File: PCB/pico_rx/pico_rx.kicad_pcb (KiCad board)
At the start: 2 copper layers, 54.6 x 89.5 mm, 77 parts, among them J1 Speaker, J2 Headphone, J4 I2C Display, J5 Antenna, J6 Battery, SW1 RotaryEncoder_Switch, SW2 SW_Push, SW3 SW_Push, SW4 SW_SPDT, U1 74CBT3251, U2 74CBT3251, U3 LTC6227, U4 FST3253, U5 Pico, U6 LTC6226xS8

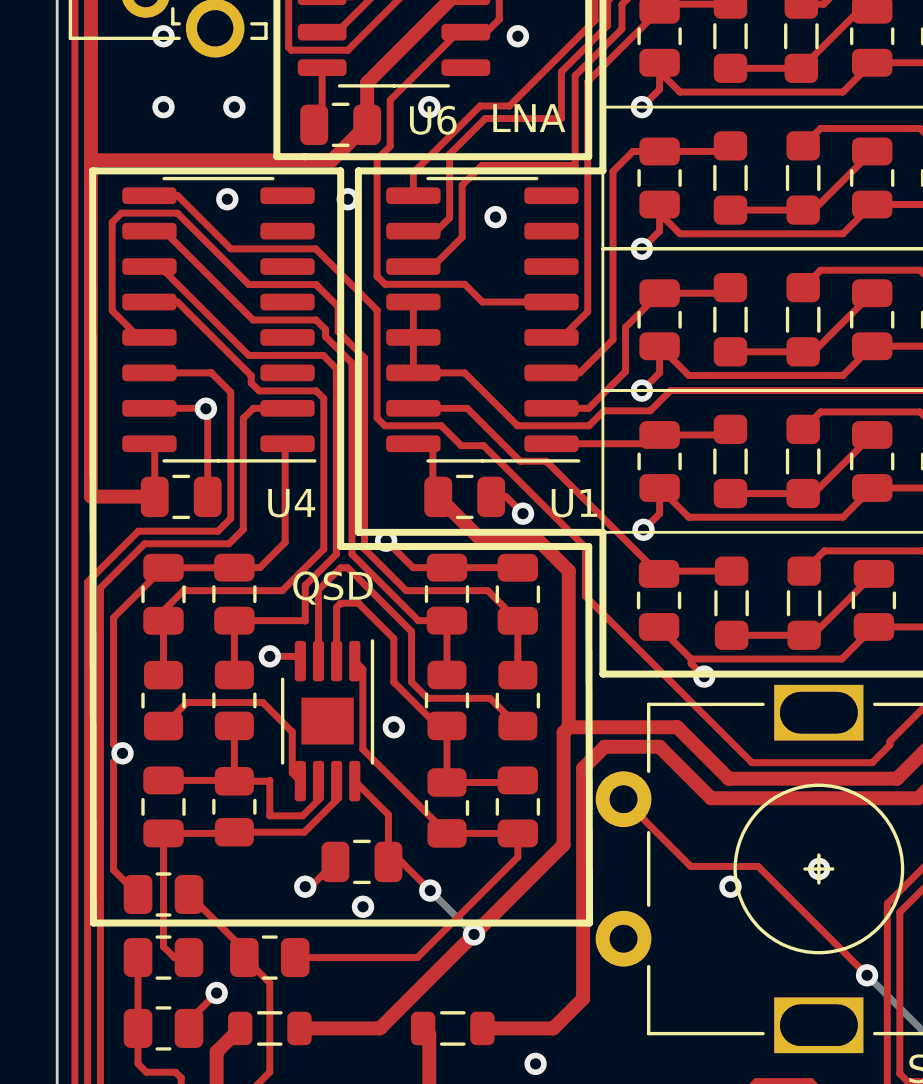
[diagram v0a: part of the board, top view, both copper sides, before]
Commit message: Correct error in schematic
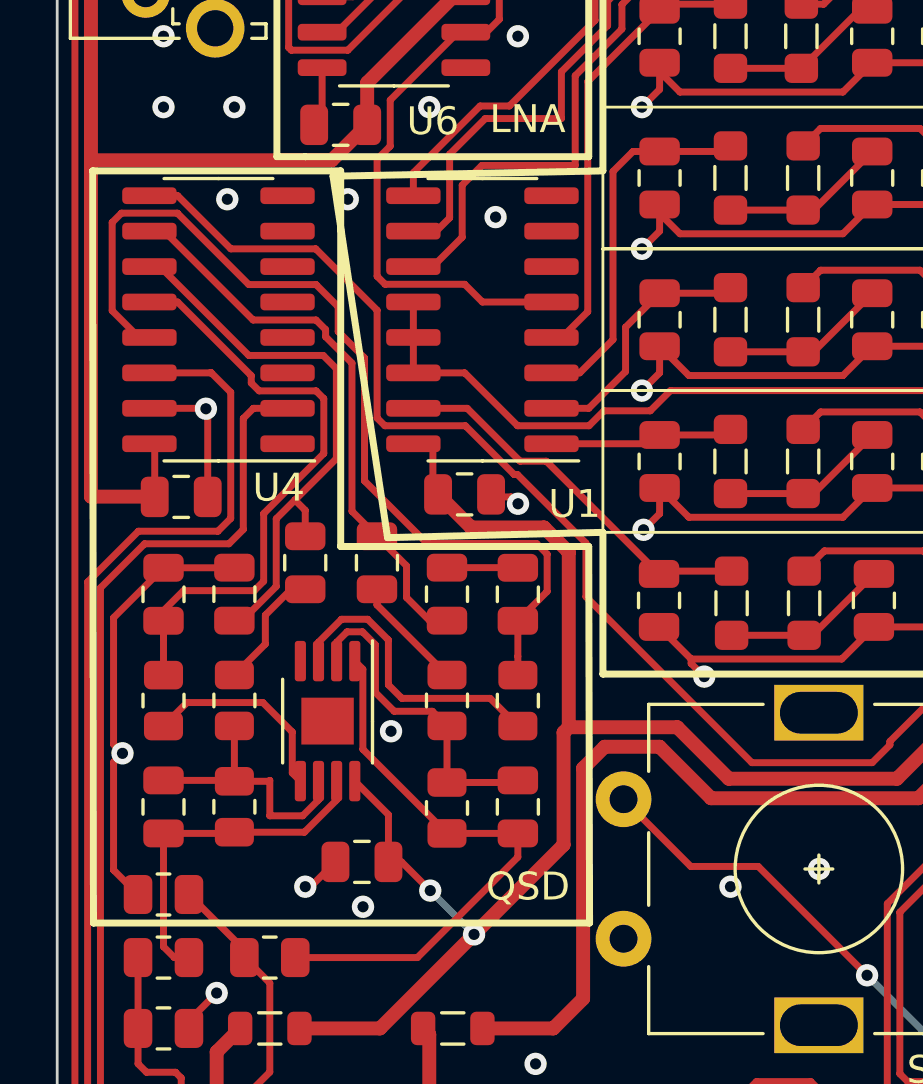
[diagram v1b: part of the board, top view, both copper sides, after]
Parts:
- added C11: 10u, Capacitor_SMD:C_0805_2012Metric, F.Cu at (111.8, 138.2)
- added C4: 10u, Capacitor_SMD:C_0805_2012Metric, F.Cu at (109.2, 138.2)
- C26, C27, C28, C29: value 27n -> 15n
- C34: value 100n -> 470n
- C5: value 10p -> 22p
- R11: value 500 -> 220
- moved C2 0.09 mm to (114.9, 135.8)
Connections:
- R3 pad 2: Net-(U4-2B2) -> Net-(C4-Pad1)
- R5 pad 2: Net-(U4-2B1) -> Net-(C11-Pad1)
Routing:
- net GND: track 123.8 -> 114.1 mm, vias 243 -> 241
- net Net-(C4-Pad1): track 0.00 -> 4.42 mm
- net Net-(C11-Pad1): track 0.00 -> 4.11 mm
- net Net-(U3A-+): track 13.4 -> 10.7 mm
- net Net-(U4-2B1): track 22.6 -> 20.4 mm
- net Net-(U4-2B2): track 22.2 -> 20.4 mm
- net Net-(U3A--): track 13.3 -> 11.8 mm
- net Net-(U4-2B4): track 32.1 -> 33.6 mm
- net Net-(U4-2B3): track 22.9 -> 22.3 mm

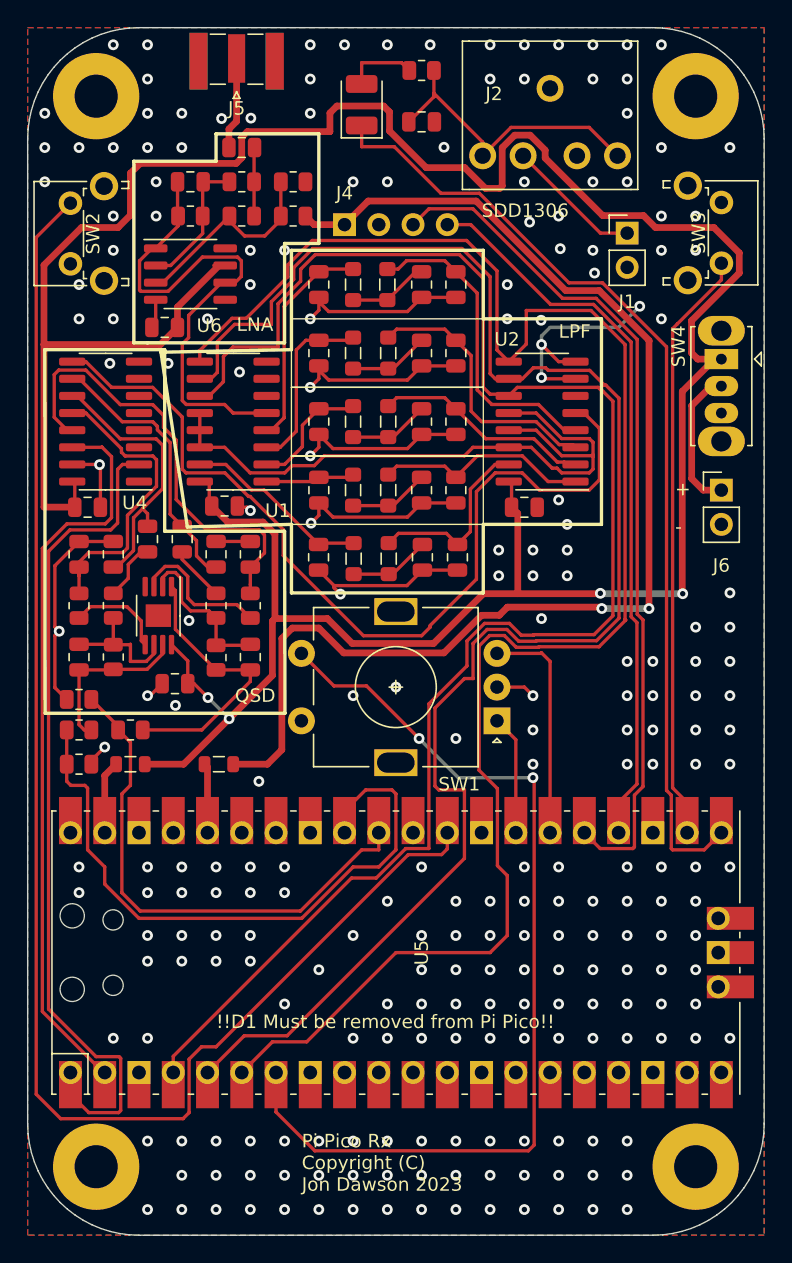
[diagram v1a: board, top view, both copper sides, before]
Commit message: Improve frequency resolution by making small adjustments to system clock. Add utility to upload memory contents over USB
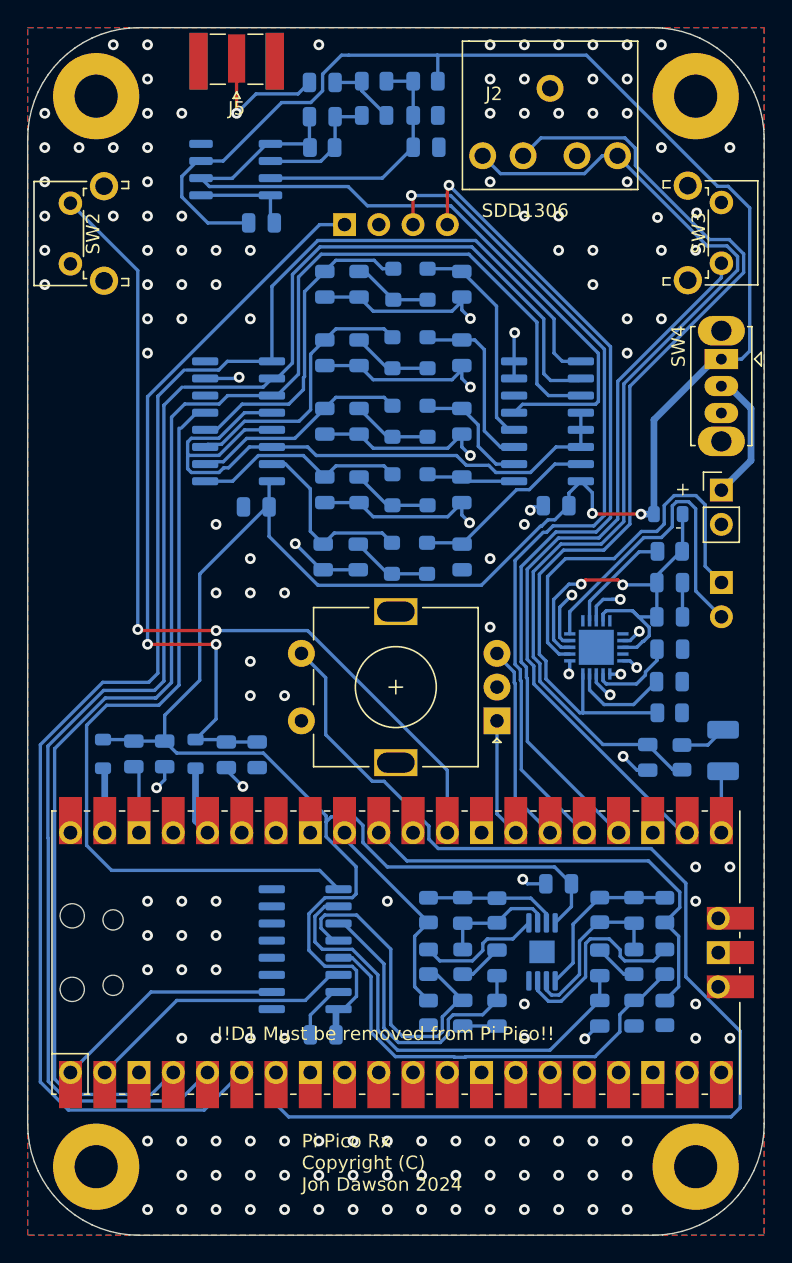
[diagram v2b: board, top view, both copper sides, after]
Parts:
- removed J1: Speaker, Connector_PinHeader_2.54mm:PinHeader_1x02_P2.54mm_Vertical
- added C17: 100n, Capacitor_SMD:C_0805_2012Metric, B.Cu at (129.9, 109.2)
- added C18: 1u, Capacitor_SMD:C_0805_2012Metric, B.Cu at (147.9, 141.5)
- added C20: 10u, Capacitor_SMD:C_0805_2012Metric, B.Cu at (147.9, 144.0)
- added C23: 1u, Capacitor_SMD:C_0805_2012Metric, B.Cu at (147.9, 148.8)
- added C32: 1u, Capacitor_SMD:C_0805_2012Metric, B.Cu at (147.9, 146.4)
- added C33: 10u, Capacitor_SMD:C_0805_2012Metric, B.Cu at (115.1, 154.2)
- added C35: 100n, Capacitor_SMD:C_0805_2012Metric, B.Cu at (110.5, 154.2)
- added C40: 10u, Capacitor_SMD:C_0805_2012Metric, B.Cu at (108.2, 154.2)
- added C41: 100n, Capacitor_SMD:C_0805_2012Metric, B.Cu at (117.3, 154.2)
- added FB3: Ferrite_Bead, Inductor_SMD:L_0805_2012Metric, B.Cu at (147.8, 136.4)
- added J3: speaker, Connector_PinHeader_2.54mm:PinHeader_1x02_P2.54mm_Vertical, B.Cu at (151.8, 141.5)
- added R17: 1k, Resistor_SMD:R_0805_2012Metric, B.Cu at (147.9, 151.1)
- added R18: 100K, Resistor_SMD:R_0805_2012Metric, B.Cu at (147.9, 139.2)
- added U7: TPA2012D2RTJT, reciever:QFN50P400X400X80-21N270X270, B.Cu at (142.5, 146.3)
- C1, C10, C11, C12, C13, C14, C15, C16, C19, C2, C21, C22, C24, C25, C26, C27, C28, C29, C3, C30, C31, C34, C36, C37, C38, C39, C4, C5, C6, C7, C8, C9, FB1, FB2, L1, L13, L2, L3, L4, L5, L6, L7, L8, L9, R1, R10, R11, R12, R13, R14, R15, R16, R2, R3, R4, R5, R6, R7, R8, R9, U1, U2, U3, U4, U6: moved to B.Cu
- moved C39 54.9 mm to (151.9, 153.9)
- moved R9 54.5 mm to (148.8, 154.4), turned to -90 degrees
- moved C34 50.0 mm to (146.3, 154.4), turned to -90 degrees
- moved R15 49.3 mm to (147.6, 173.4), turned to 90 degrees
- moved C27 44.4 mm to (142.7, 173.4), turned to 90 degrees
- moved C26 44.4 mm to (135.1, 173.4), turned to 90 degrees
- moved C29 44.3 mm to (145.3, 173.4), turned to 90 degrees
- moved C28 44.3 mm to (132.6, 173.4), turned to 90 degrees
- moved C11 44.1 mm to (142.7, 169.7), turned to -90 degrees
- moved C25 42.8 mm to (122.2, 175.0), turned to 180 degrees
- moved U4 41.8 mm to (120.9, 168.7), turned to 0 degrees
- moved R14 41.8 mm to (147.6, 165.8), turned to 90 degrees
- moved C4 40.7 mm to (135.1, 169.7), turned to -90 degrees
- moved R5 40.7 mm to (145.3, 169.6), turned to -90 degrees
- moved R6 40.5 mm to (147.6, 169.6), turned to -90 degrees
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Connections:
- J2 pad TN: Net-(J1-Pin_1) -> AUDIO_AMPLIFIER
- R2 pad 1: +3V3 -> +5V
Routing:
- net AUDIO_AMPLIFIER: track 0.00 -> 73.1 mm
- net SPEAKER: track 71.9 -> 4.61 mm
- net Net-(C34-Pad1): track 22.5 -> 76.1 mm
- net LO_Q: track 62.3 -> 17.4 mm
- net /PI Pico/BUTTON_FWD: track 110.2 -> 65.6 mm, vias 0 -> 2
- net +3V3: track 92.7 -> 55.7 mm
- net LO_I: track 54.6 -> 20.3 mm
- net Net-(U5-GPIO27_ADC1): track 48.3 -> 15.4 mm
- net Net-(U7-AVDD): track 0.00 -> 30.4 mm, vias 0 -> 2
- net Net-(J3-Pin_1): track 0.00 -> 28.4 mm
- net Net-(J3-Pin_2): track 0.00 -> 24.3 mm
- net /PI Pico/PUSH: track 71.7 -> 94.4 mm, vias 2 -> 0
- net RF_PREAMP: track 37.3 -> 56.3 mm
- net Net-(U4-2B1): track 20.4 -> 34.2 mm
- net /PI Pico/BUTTON_BACK: track 44.2 -> 55.0 mm
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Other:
- board text added: "Pi Pico Rx Copyright (C) Jon Dawson 2024"
- board text removed: "I"
- board text removed: "Pi Pico Rx Copyright (C) Jon Dawson 2023"
- board text removed: "Q"
- board text removed: "QSD"

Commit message: Update PCB design to fix issues found
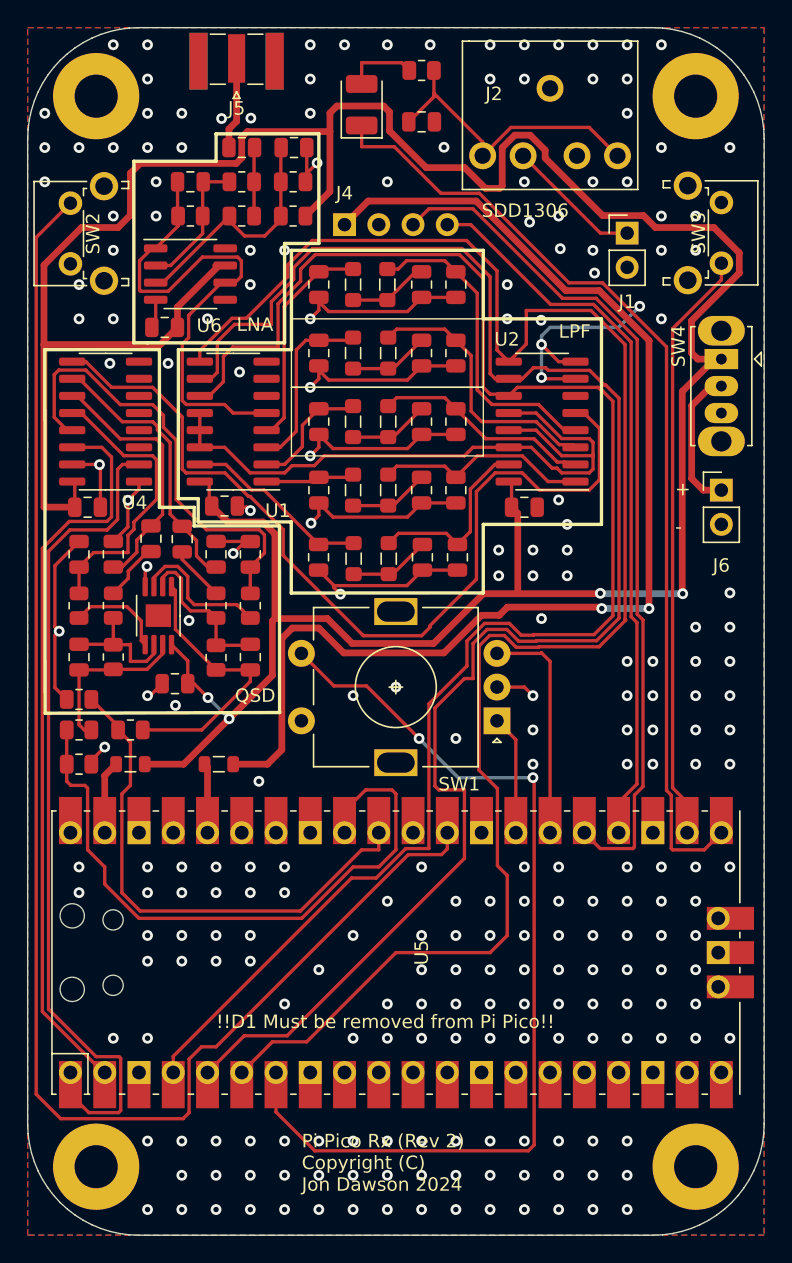
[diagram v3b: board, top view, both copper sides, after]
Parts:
- removed C18, C23, C32: 1u, Capacitor_SMD:C_0805_2012Metric
- removed C20, C33, C40: 10u, Capacitor_SMD:C_0805_2012Metric
- removed C35, C41: 100n, Capacitor_SMD:C_0805_2012Metric
- removed FB3: Ferrite_Bead, Inductor_SMD:L_0805_2012Metric
- removed J3: speaker, Connector_PinHeader_2.54mm:PinHeader_1x02_P2.54mm_Vertical
- removed R17: 1k, Resistor_SMD:R_0805_2012Metric
- removed R18: 100K, Resistor_SMD:R_0805_2012Metric
- removed U7: TPA2012D2RTJT, reciever:QFN50P400X400X80-21N270X270
- added J1: Speaker, Connector_PinHeader_2.54mm:PinHeader_1x02_P2.54mm_Vertical, F.Cu at (144.8, 115.6)
- C1: value 100n -> 10n; moved to F.Cu
- C10, C11, C12, C13, C14, C15, C16, C17, C19, C2, C21, C22, C24, C25, C26, C27, C28, C29, C3, C30, C31, C34, C36, C37, C38, C39, C4, C5, C6, C7, C8, C9, FB1, FB2, L1, L13, L2, L3, L4, L5, L6, L7, L8, L9, R10, R11, R13, R14, R15, R16, R2, R3, R4, R5, R6, R7, R8, R9, U1, U2, U3, U4, U6: moved to F.Cu
- R1: value 50 -> 47; moved to F.Cu
- R12: value 0 -> 1k; moved to F.Cu
- moved C39 54.9 mm to (125.1, 106.0)
- moved R9 54.5 mm to (129.5, 103.5), turned to 0 degrees
- moved C34 50.0 mm to (129.5, 107.3), turned to 0 degrees
- moved R15 49.3 mm to (104.1, 150.1), turned to 0 degrees
- moved C27 44.4 mm to (114.3, 139.4), turned to -90 degrees
- moved C26 44.4 mm to (106.7, 139.4), turned to -90 degrees
- moved C29 44.3 mm to (116.8, 139.4), turned to -90 degrees
- moved C28 44.3 mm to (104.1, 139.4), turned to -90 degrees
- moved C11 44.1 mm to (111.8, 138.2), turned to 90 degrees
- moved C25 42.8 mm to (104.8, 135.9), turned to 0 degrees
- moved U4 41.8 mm to (106.1, 129.5), turned to 180 degrees
- moved R14 41.8 mm to (108.0, 152.4), turned to 0 degrees
- moved R5 40.7 mm to (114.3, 143.2), turned to 90 degrees
- moved C4 40.6 mm to (109.5, 138.2), turned to 90 degrees
- moved R6 40.5 mm to (116.8, 143.2), turned to 90 degrees
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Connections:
- J2 pad TN: AUDIO_AMPLIFIER -> Net-(J1-Pin_1)
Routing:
- net AUDIO_AMPLIFIER: track 73.1 -> 0.00 mm
- net SPEAKER: track 4.61 -> 71.9 mm
- net Net-(C34-Pad1): track 76.1 -> 22.5 mm
- net LO_Q: track 17.4 -> 62.2 mm
- net /PI Pico/BUTTON_FWD: track 65.6 -> 110.2 mm, vias 2 -> 0
- net LO_I: track 20.3 -> 54.6 mm
- net +3V3: track 55.7 -> 89.5 mm
- net Net-(U5-GPIO27_ADC1): track 15.4 -> 48.3 mm
- net Net-(U7-AVDD): track 30.4 -> 0.00 mm, vias 2 -> 0
- net Net-(J3-Pin_1): track 28.4 -> 0.00 mm
- net Net-(J3-Pin_2): track 24.3 -> 0.00 mm
- net /PI Pico/PUSH: track 94.4 -> 71.7 mm, vias 0 -> 2
- net RF_PREAMP: track 56.3 -> 37.3 mm
- net GND: track 110.1 -> 124.2 mm, vias 158 -> 244
- net Net-(U4-2B1): track 34.2 -> 20.4 mm
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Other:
- board text added: "I"
- board text added: "Pi Pico Rx (Rev 2) Copyright (C) Jon Dawson 2024"
- board text added: "Q"
- board text added: "QSD"
- board text removed: "Pi Pico Rx Copyright (C) Jon Dawson 2024"
